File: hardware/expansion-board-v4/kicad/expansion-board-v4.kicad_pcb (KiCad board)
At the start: 6 copper layers, 100 x 62 mm, 182 parts, among them J1 PinHeader_2x20_P2.54mm_Vertic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, J2 U.FL_Hirose_U.FL-R-SMT-1_Vert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, J4 USB_C_Receptacle_HRO_TYPE-C-3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, J5 U.FL_Hirose_U.FL-R-SMT-1_Vert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, J6 U.FL_Hirose_U.FL-R-SMT-1_Vert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, J7 U.FL_Hirose_U.FL-R-SMT-1_Vert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, J8 U.FL_Hirose_U.FL-R-SMT-1_Vert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, J9 MX1.25WT-2P, Q2 SOT-23, Q3 SOT-23, Q4 SOT-23, Q5 SOT-23, SW1 SolderJumper-2_P1.3mm_Open_Pa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, SW2 SolderJumper-2_P1.3mm_Open_Pa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, U1 SOT-23-5, U10 QFN-48-1EP_7x7mm_P0.5mm_EP5.1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, U11 DFN-8-1EP_2x2mm_P0.5mm_EP0.86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, U12 SOT-363_SC-70-6, U13 AD8319_LFCSP-8-EP, U14 MSOP-8_3x3mm_P0.65mm, U15 SOT-23-6, U16 SOT-363_SC-70-6, U17 SOT-363_SC-70-6, U18 SOIC-10_3.9x4.9mm_P1mm, U19 QFN-24-1EP_4x4mm_P0.5mm_EP2.6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, U2 SOT-23-5, U20 TSOT-23-6, U3 SOT-23-5, U4 BNO085_LGA-28, U5 BMP388_LGA-10, U6 LGA-16_3x3mm_P0.5mm, U7 ATGM336H_LCC-18, U8 QFN-56-1EP_7x7mm_P0.4mm_EP3.2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, U9 SOIC-8_5.3x5.3mm_P1.27mm, Y1 Crystal_SMD_3225-4Pin_3.2x2.5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, Y2 Crystal_SMD_3225-4Pin_3.2x2.5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, Y3 Crystal_SMD_3215-2Pin_3.2x1.5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

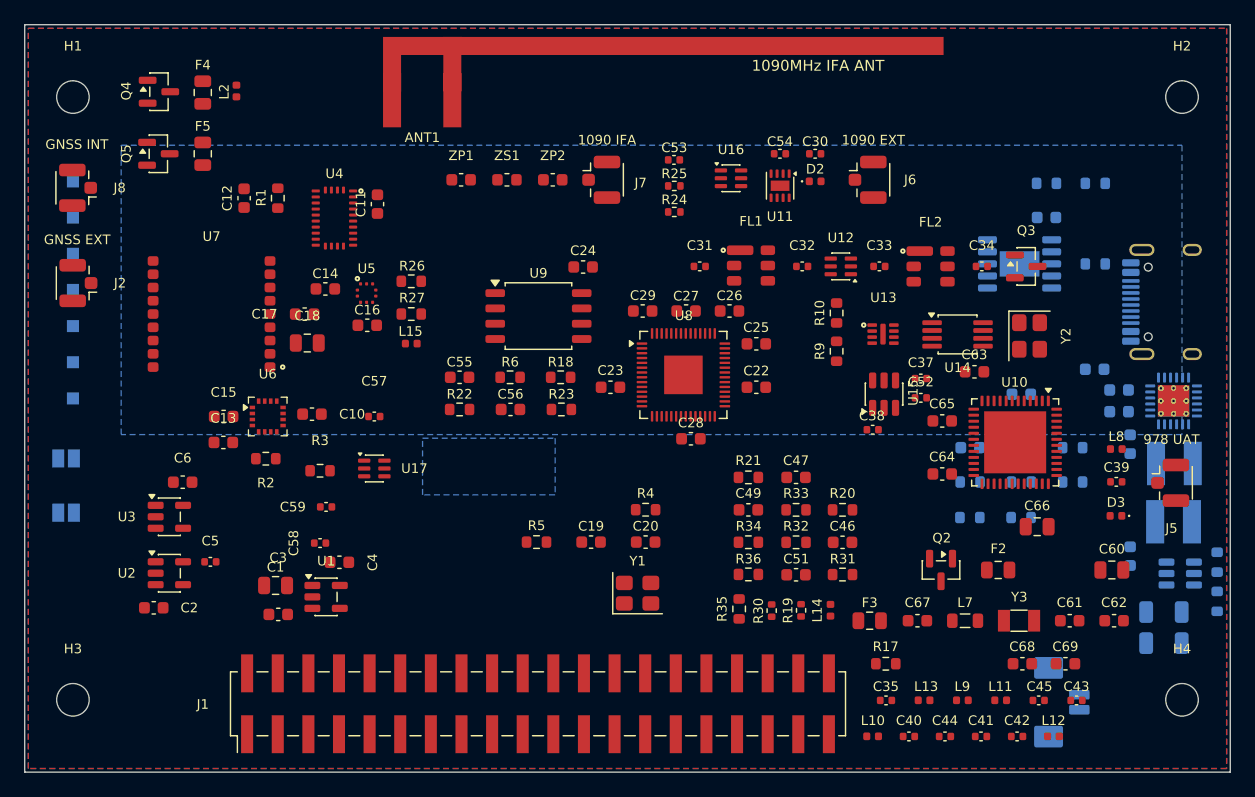
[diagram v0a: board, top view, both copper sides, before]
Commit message: fix(hw): F 面丝印 57 处缺陷清零，含 26 处压焊盘
F 面丝印此前没经过人工整理（人工整理的是 B 面），实测：
  压开窗焊盘 26 处、位号重叠 12 处、压别人本体 17 处
丝印油墨上锡盘工厂会投诉，这是必须清掉的。

新增 tools/check_silk.py 做体检，7 项。过程中修掉三个判据错误——
判据错了比不判更浪费时间：

  · 「压本体」原本拿 courtyard 判。0603 的 courtyard 比本体每边大
    0.25mm，密排网格上刷出一堆假阳性（B 面 4 处，实测每处只压进
    0.094mm，离本体还有 0.156mm）。改用 Fab 层真实轮廓。
  · 「压焊盘」原本不分是否开阻焊窗。ANT1 的 pin1 是 45x7.5mm 的 IFA
    辐射臂，只有 F.Cu 没有 F.Mask，天线附近每个位号都「压」上它，
    5 个误报把真正的 3 处淹掉了。改成只算开窗的可焊焊盘。
  · 「离元件太远」原本用位号中心到本体中心的距离。J1 是 2x20 排针、
    本体 50mm 宽，位号紧贴短边到中心也有 26mm——一个完全正确的摆放
    被报成缺陷。改用矩形边界间距。

新增 tools/place_ref.py 做近位搜索，比 gen_silk 的试位多一个自由度：
允许把字号从 0.8 缩到 0.6（厂家能力内），用一点可读性换「位号贴着
自己的元件」。gen_silk 找不到位就往几毫米外甩，返修的人会按最近原则
认错主人。

天线辐射臂单独设为丝印禁区：它不开阻焊窗所以不算「焊盘」，但丝印油墨
εr≈3~4、厚 10~20µm 会拉低 IFA 谐振点。原来有 5 个位号落在上面。

另外做了同区域位置交换（tools/swap_opt.py）：只交换、不产生新坐标，
所以人工排好的网格和分区零损失。收益有限（交叉 856→834），因为交叉
是拓扑造成的不是小件摆放造成的——分析和取舍见 REVIEW_TODO.md。

验收：F/B 两面丝印检测全通过，DRC error 0 条，覆铜已填。
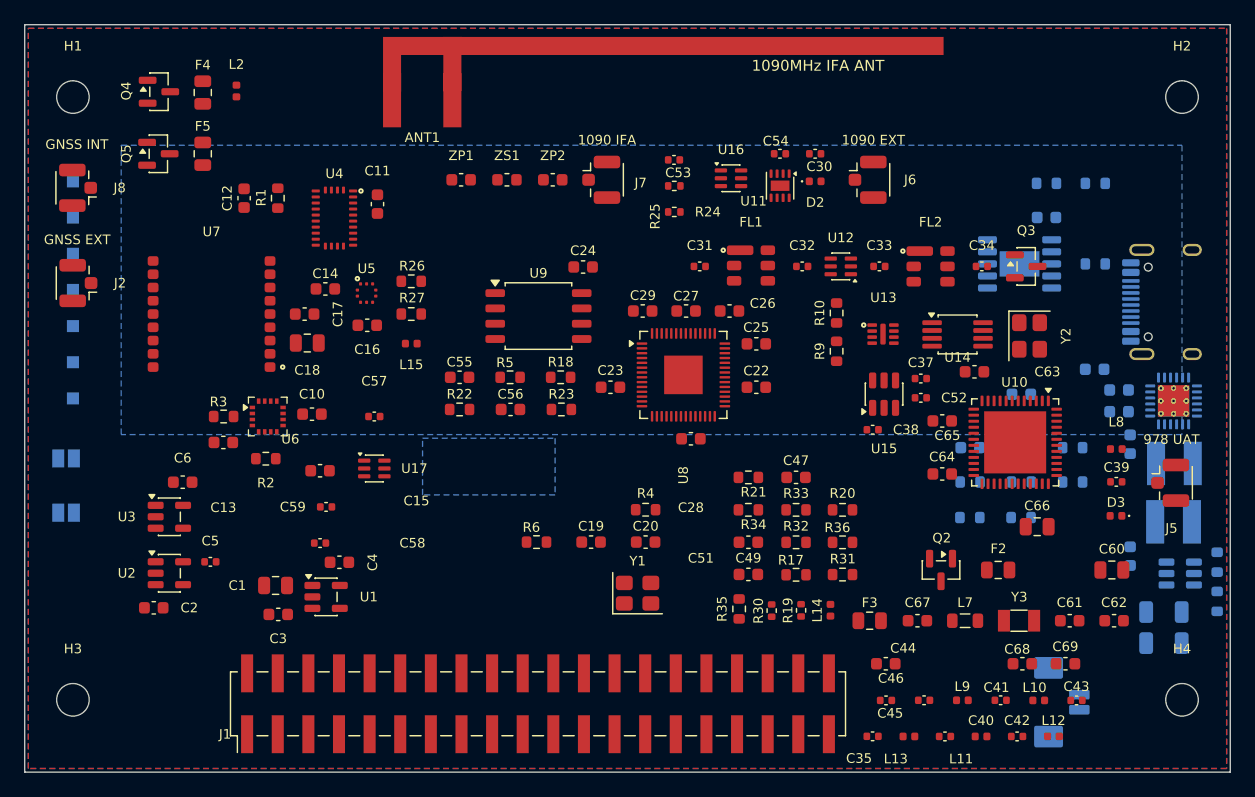
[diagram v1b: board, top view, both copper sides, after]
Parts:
- moved L10 14.1 mm to (134.1, 106.0)
- moved R6 13.8 mm to (92.5, 92.9)
- moved R5 13.8 mm to (90.3, 79.2)
- moved C45 12.7 mm to (121.4, 106.0)
- moved C46 10.7 mm to (121.4, 103.0)
- moved R17 10.5 mm to (114.0, 95.6)
- moved C15 9.18 mm to (74.5, 87.0)
- moved R3 9.18 mm to (66.5, 82.5)
- moved R36 8.25 mm to (117.8, 92.9)
- moved C51 3.96 mm to (110.0, 95.6)
- moved C44 3.46 mm to (124.6, 106.0)
- moved C41 3.41 mm to (131.0, 106.0)
- moved L11 3.41 mm to (129.3, 109.0)
- moved L13 3.25 mm to (123.3, 109.0)
- moved C35 3.18 mm to (120.3, 109.0)
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
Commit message: fix(hw): 测试点搬到信号源对面，交叉 834→700、QSPI 片选 stub 36→6mm
起因是一句质疑：「这些 TP 是否真的那么重要？只是首次打板用的吧？」
我之前把「TP 摆哪」当成需要权衡的约束，没先问「还要不要」。查完发现
问题问错了方向——这 7 条网络每条只有 2 个节点：

    DEMOD0  →  TP3.1, U8.31        SWCLK  →  TP1.1, U8.24
    DEMOD1  →  TP4.1, U8.32        SWDIO  →  TP2.1, U8.25

没有第三方。这 7 条 54mm 飞线存在的唯一理由就是测试点自己，而且全部
横穿 J1 那 40 根信号线。SWD 也不是烧录必需：RP2040 的 USB 接到 J4，
按 BOOTSEL 拖 UF2 就能刷。

顺带查出一个跟 TP 无关的真缺陷：SW2 不是单纯的短接焊盘，QSPI_SS 是
RP2040 到 Flash 的**片选线**，SW2 在 x52.8 等于给这条总线挂了 36mm
stub（对比 QSPI_SCLK 全长才 7.4mm）。RP2040 跑 XIP 时 QSPI 最高
133MHz，这会吃掉时序余量。已挪到 U8 与 U9 之间，stub 36→6.1mm；
RP_RUN 的 stub 33→3.0mm。

修掉自己两个脚本里的同一个 bug：FOOTPRINT.SetPosition() 本身就会带着
Reference 一起移动，我又手动加了一次位移，等于双倍——TP1–7 的位号
因此被甩到 x152~167，而板宽只到 150。move_testpoints.py 和
swap_opt.py 都有这处错误。

⚠️ 未决：电池 955465 是 65×54，B 面可用 x 区间只有 57.5–142.5，
无论怎么摆 x105 这一列都在它投影下——TP 和电池是硬冲突，不存在两全的
位置。实测删掉 TP3–7 反而比搬过去更好（交叉 670 vs 700）且不占电池
的地方。删元件不可逆，等确认，板子暂停在「搬过去」这个状态。
详见 REVIEW_TODO.md 的 A 节。

验收：F/B 丝印检测通过（B 面剩 0.014mm 擦边一处），DRC error 0 条。
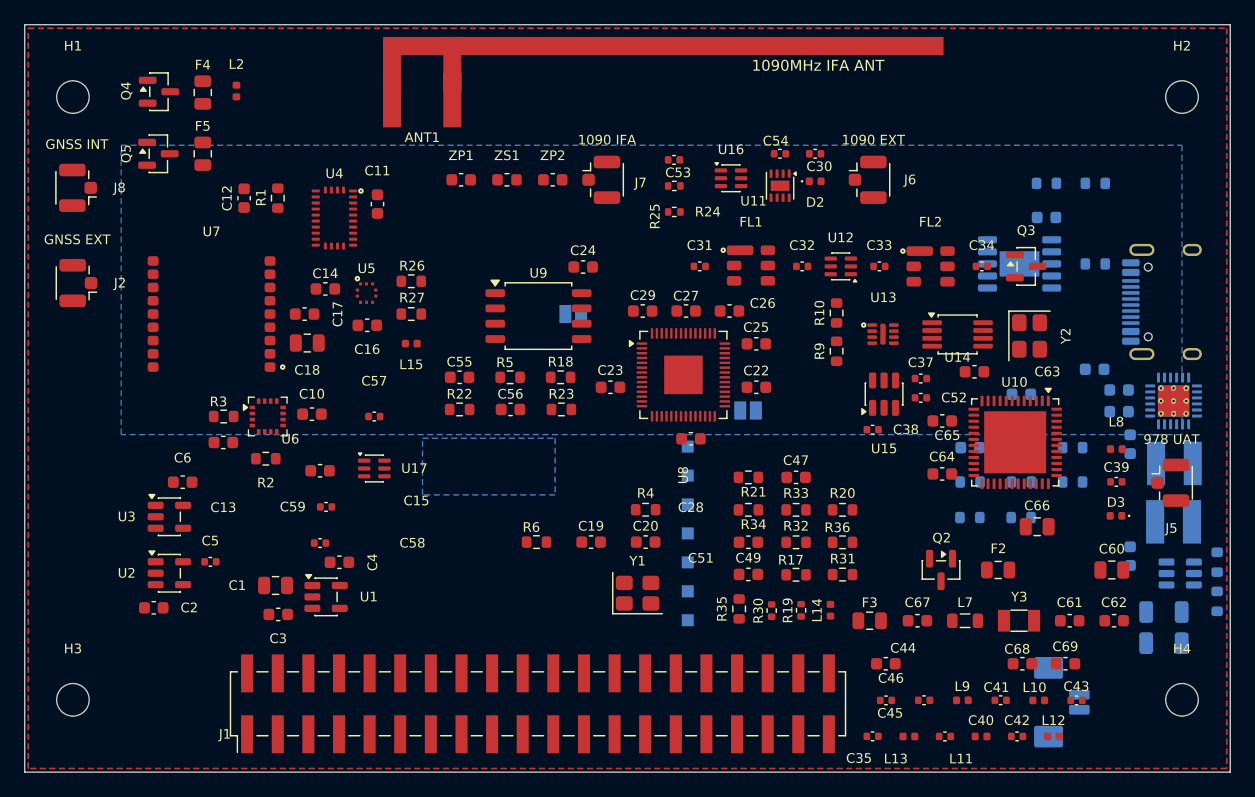
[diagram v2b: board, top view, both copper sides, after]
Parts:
- moved SW1 56.7 mm to (110.0, 82.0)
- moved TP1 55.5 mm to (105.0, 85.0)
- moved TP2 55.3 mm to (105.0, 87.4)
- moved TP3 55.1 mm to (105.0, 89.8)
- moved TP4 54.9 mm to (105.0, 92.2)
- moved TP5 54.6 mm to (105.0, 94.6)
- moved TP6 54.4 mm to (105.0, 97.0)
- moved TP7 54.2 mm to (105.0, 99.4)
- moved SW2 45.2 mm to (95.5, 74.0)
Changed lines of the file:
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@@
 	(footprint "TestPoint_Pad_1.0x1.0mm"
 		(layer "B.Cu")
-		(at 54 66)
+		(at 105 87.4)
 		(descr "SMD rectangular pad as test Point, square 1.0mm side length")
 		(tags "test point SMD pad rectangle square")
 		(property "Reference" "TP2"
-			(at -2.256 0.001999 0)
+			(at 1.895 0 0)
 			(layer "B.SilkS")
 			(effects
 				(font
 					(size 0.8 0.8)
-					(thickness 0.15)
+					(thickness 0.136)
 				)
 				(justify mirror)
@@
 	(footprint "TestPoint_Pad_1.0x1.0mm"
 		(layer "B.Cu")
-		(at 54 75)
+		(at 105 94.6)
 		(descr "SMD rectangular pad as test Point, square 1.0mm side length")
 		(tags "test point SMD pad rectangle square")
 		(property "Reference" "TP5"
-			(at -2.256 0.007 0)
+			(at 1.895 0 0)
 			(layer "B.SilkS")
 			(effects
 				(font
 					(size 0.8 0.8)
-					(thickness 0.15)
+					(thickness 0.136)
 				)
 				(justify mirror)
@@
 	(footprint "TestPoint_Pad_1.0x1.0mm"
 		(layer "B.Cu")
-		(at 54 69)
+		(at 105 89.8)
 		(descr "SMD rectangular pad as test Point, square 1.0mm side length")
 		(tags "test point SMD pad rectangle square")
 		(property "Reference" "TP3"
-			(at -2.256 0.003 0)
+			(at 1.895 0 0)
 			(layer "B.SilkS")
 			(effects
 				(font
 					(size 0.8 0.8)
-					(thickness 0.15)
+					(thickness 0.136)
 				)
 				(justify mirror)
@@
 	(footprint "TestPoint_Pad_1.0x1.0mm"
 		(layer "B.Cu")
-		(at 54 63)
+		(at 105 85)
 		(descr "SMD rectangular pad as test Point, square 1.0mm side length")
 		(tags "test point SMD pad rectangle square")
 		(property "Reference" "TP1"
-			(at -2.256 0 0)
+			(at -0.348 -1.299 0)
 			(layer "B.SilkS")
 			(effects
 				(font
 					(size 0.8 0.8)
-					(thickness 0.15)
+					(thickness 0.136)
 				)
 				(justify mirror)
@@
 	(footprint "TestPoint_Pad_1.0x1.0mm"
 		(layer "B.Cu")
-		(at 54 81)
+		(at 105 99.4)
 		(descr "SMD rectangular pad as test Point, square 1.0mm side length")
 		(tags "test point SMD pad rectangle square")
 		(property "Reference" "TP7"
-			(at -2.256 0.01 0)
+			(at 0.348 1.299 0)
 			(layer "B.SilkS")
 			(effects
 				(font
 					(size 0.8 0.8)
-					(thickness 0.15)
+					(thickness 0.136)
 				)
 				(justify mirror)
@@
 	(footprint "TestPoint_Pad_1.0x1.0mm"
 		(layer "B.Cu")
-		(at 54 78)
+		(at 105 97)
 		(descr "SMD rectangular pad as test Point, square 1.0mm side length")
 		(tags "test point SMD pad rectangle square")
 		(property "Reference" "TP6"
-			(at -2.256 0.008 0)
+			(at 1.895 0 0)
 			(layer "B.SilkS")
 			(effects
 				(font
 					(size 0.8 0.8)
-					(thickness 0.15)
+					(thickness 0.136)
 				)
 				(justify mirror)
@@
 	(footprint "SolderJumper-2_P1.3mm_Open_Pad1.0x1.5mm"
 		(layer "B.Cu")
-		(at 53.43 85.98)
+		(at 110 82)
 		(descr "SMD Solder Jumper, 1x1.5mm Pads, 0.3mm gap, open")
 		(tags "solder jumper open")
 		(property "Reference" "SW1"
-			(at -0.03 -1.75 0)
+			(at 0.516 1.541 0)
 			(layer "B.SilkS")
 			(effects
 				(font
 					(size 0.8 0.8)
-					(thickness 0.15)
+					(thickness 0.136)
 				)
 				(justify mirror)
@@
 	(footprint "TestPoint_Pad_1.0x1.0mm"
 		(layer "B.Cu")
-		(at 54 72)
+		(at 105 92.2)
 		(descr "SMD rectangular pad as test Point, square 1.0mm side length")
 		(tags "test point SMD pad rectangle square")
 		(property "Reference" "TP4"
-			(at -2.256 0.005 0)
+			(at 1.895 0 0)
 			(layer "B.SilkS")
 			(effects
 				(font
 					(size 0.8 0.8)
-					(thickness 0.15)
+					(thickness 0.136)
 				)
 				(justify mirror)
@@
 	(footprint "SolderJumper-2_P1.3mm_Open_Pad1.0x1.5mm"
 		(layer "B.Cu")
-		(at 53.43 90.48)
+		(at 95.5 74)
 		(descr "SMD Solder Jumper, 1x1.5mm Pads, 0.3mm gap, open")
 		(tags "solder jumper open")
 		(property "Reference" "SW2"
-			(at -0.07 -1.72 0)
+			(at 0.516 1.541 0)
 			(layer "B.SilkS")
 			(effects
 				(font
 					(size 0.8 0.8)
-					(thickness 0.15)
+					(thickness 0.136)
 				)
 				(justify mirror)

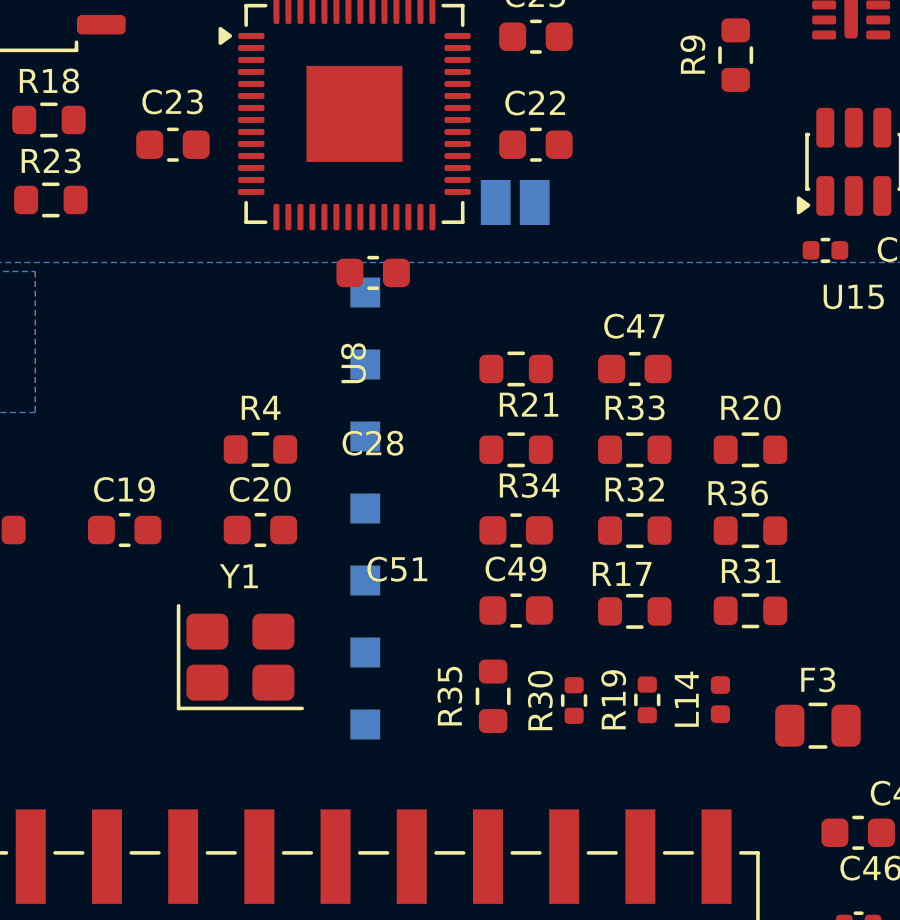
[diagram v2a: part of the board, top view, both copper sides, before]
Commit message: feat(hw): 删掉 TP1-7 与 SW1，飞线交叉 834→612、B 面中间让给电池
判据不是「省地方」，是这 7 条网络除了测试点没有第三方节点：
DEMOD0-3(GPIO20-23) 和 RECOVERED_CLK(GPIO24) 是固件里 PIO 解码状态机
往外**输出**的调试信号，不在接收链上——接收链是
AD8319 → TLV3501 比较器 → PULSES → GPIO19，一个测试点都没有。

固件调试在已打样的 v3.2 上做，那块板的 TP 和解调链与本板逐条相同
（expansion-board-v3/tools/sheet_mcu.py:95）。刷机走 USB UF2，
SWD 不是烧录必需。

SW1(RESET) 一并删掉：RUN 脚由 R5 上拉即可，复位靠断电或软件。

保留 SW2 并已搬到 U8 与 U9 之间——它是唯一的强制刷机入口，而且挂在
QSPI_SS 这条 RP2040 到 Flash 的片选线上，原来在 x52.8 等于给总线挂了
36mm stub（QSPI_SCLK 全长才 7.4mm），现在 6.1mm。

  飞线总长  3100 → 2640mm  (-15%)
  飞线交叉   834 → 612 处  (-27%)
  元件数     182 → 174
  B 面中间   完整让给电池 955465 (65x54)

GPIO20-24 的网络名保留在引脚映射表里没标 NC，将来要加回测试点补一句
s.place 即可，原理图上也还看得出这几个脚的预期用途。

验收：DRC error 0 条，F 面丝印全通过，原理图与 PCB 元件集合一致
（差集只有 H1-H4 螺丝孔），覆铜已重填。
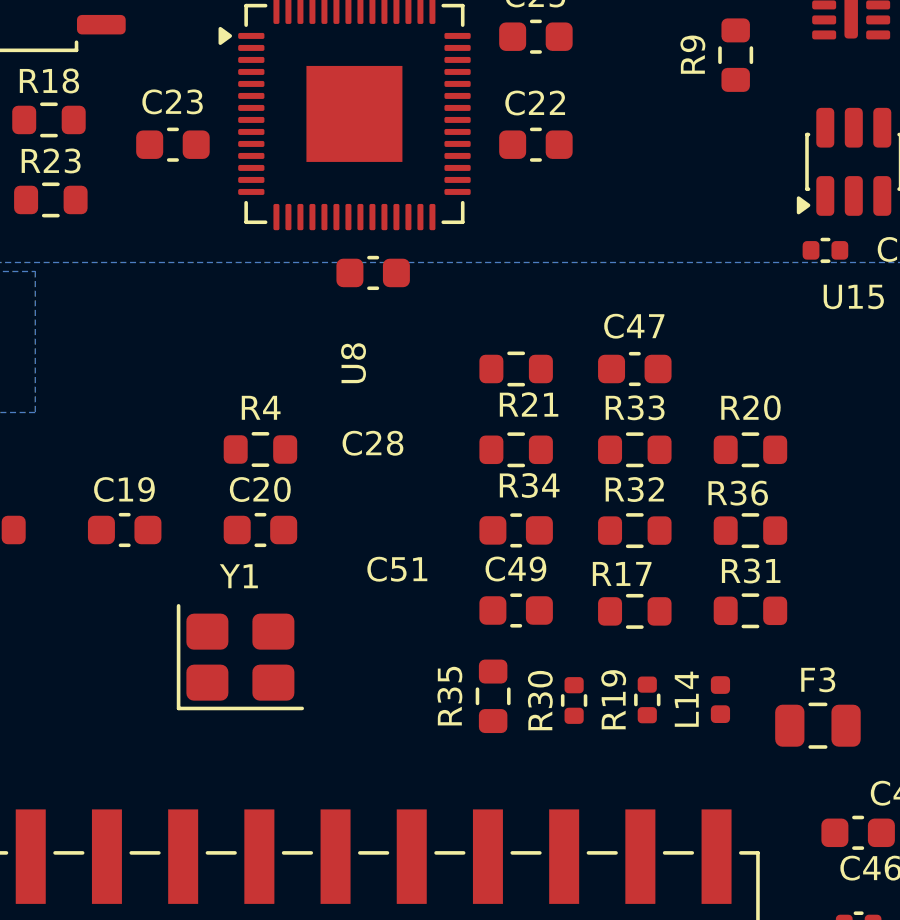
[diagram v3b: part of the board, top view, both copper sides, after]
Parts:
- removed SW1: SolderJumper-2_P1.3mm_Open_Pad1.0x1.5mm, SolderJumper-2_P1.3mm_Open_Pad1.0x1.5mm
- removed TP1, TP2, TP3, TP4, TP5, TP6, TP7: TestPoint_Pad_1.0x1.0mm, TestPoint_Pad_1.0x1.0mm
